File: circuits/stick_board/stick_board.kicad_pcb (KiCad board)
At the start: 2 copper layers, 129.2 x 50.9 mm, 22 parts, among them J1 Conn_01x13_Pin, M1 Motor_DC, M2 Motor_DC, Q1 AO3400A, Q2 AO3400A, U1 GULI, U2 GULI, U3 DRV5055A1xDBZxQ1, U4 DRV5055A1xDBZxQ1

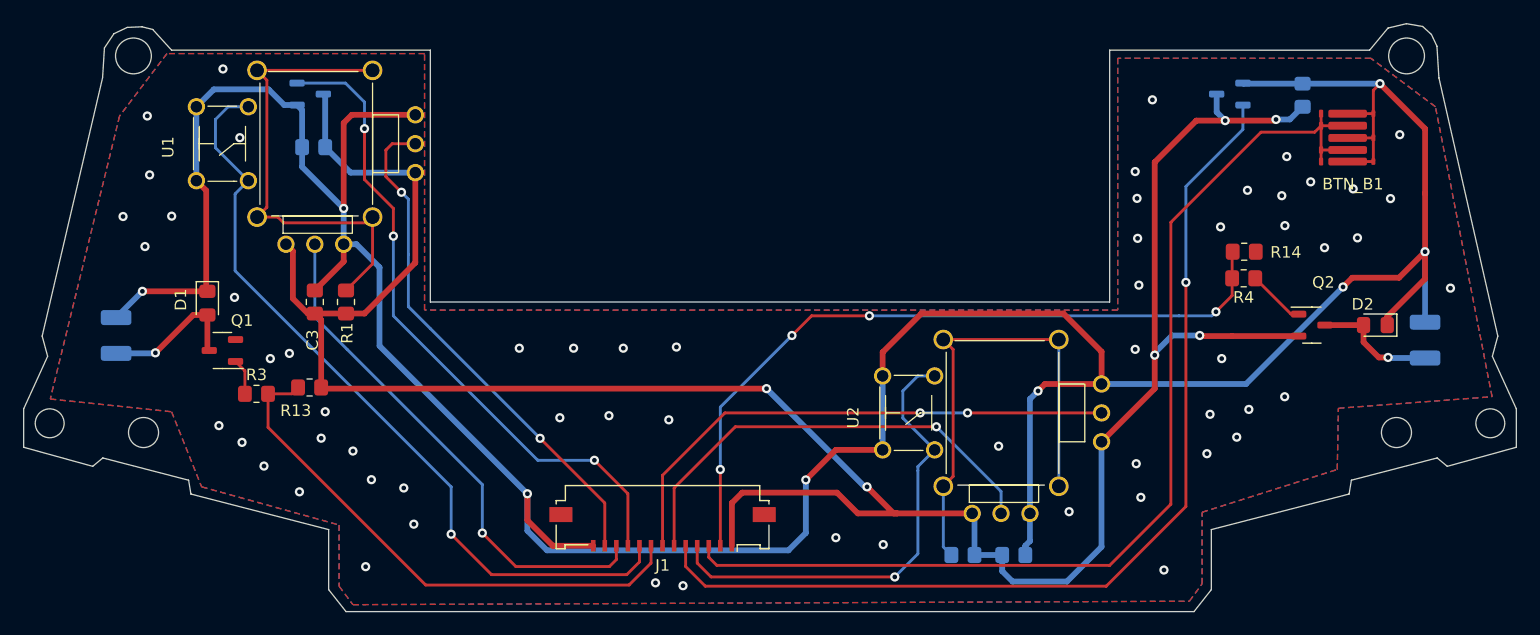
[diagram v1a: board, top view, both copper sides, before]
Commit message: 优化布局
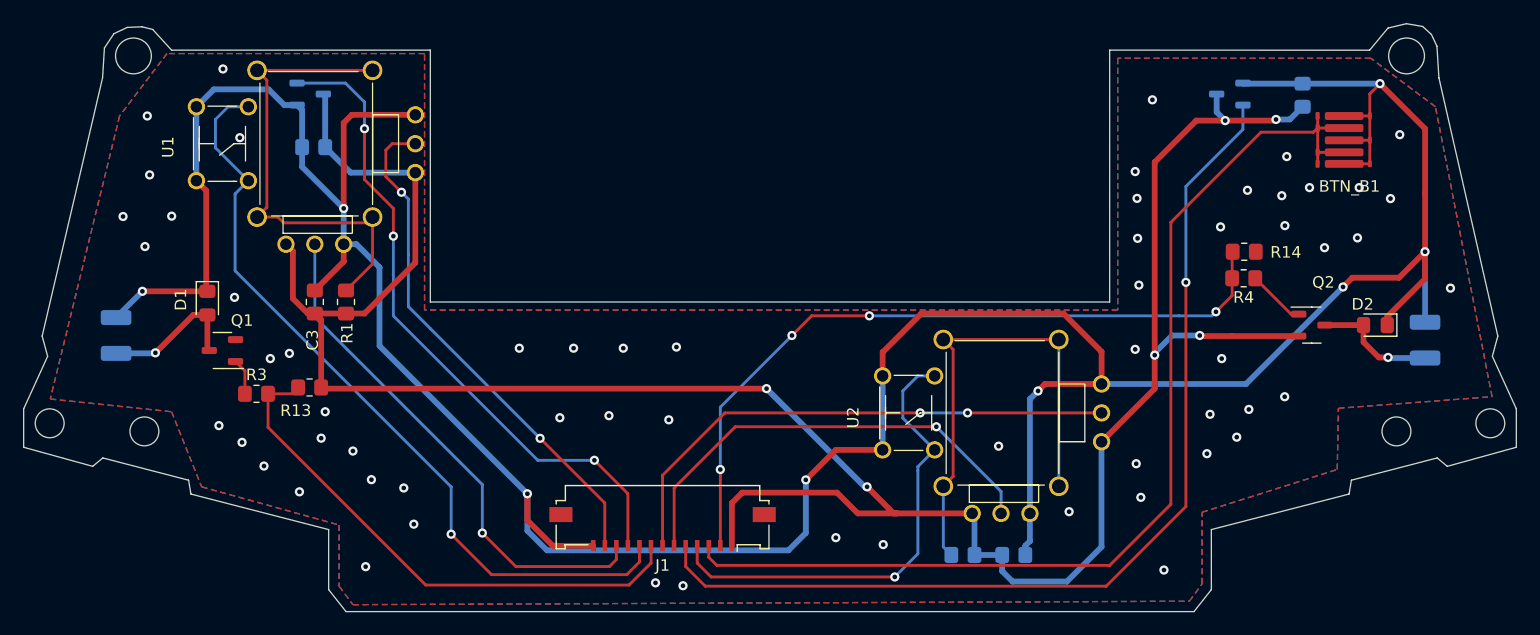
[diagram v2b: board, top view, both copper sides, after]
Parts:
- moved BTN_B1 0.36 mm to (190.8, 108.3)
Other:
- outline, holes or cut-outs redrawn
